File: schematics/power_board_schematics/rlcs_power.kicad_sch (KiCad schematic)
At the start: 40 parts, among them J1 Conn_01x05_Male, J2 Conn_01x05_Male, J3 Screw_Terminal_01x02, J4 Screw_Terminal_01x03, J5 Actuator Battery Conn, J6 Screw_Terminal_01x02, J7 Screw_Terminal_01x02, J8 Keylock Switch Conn, J9 Screw_Terminal_01x03, Q1 Q_NPN_BEC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

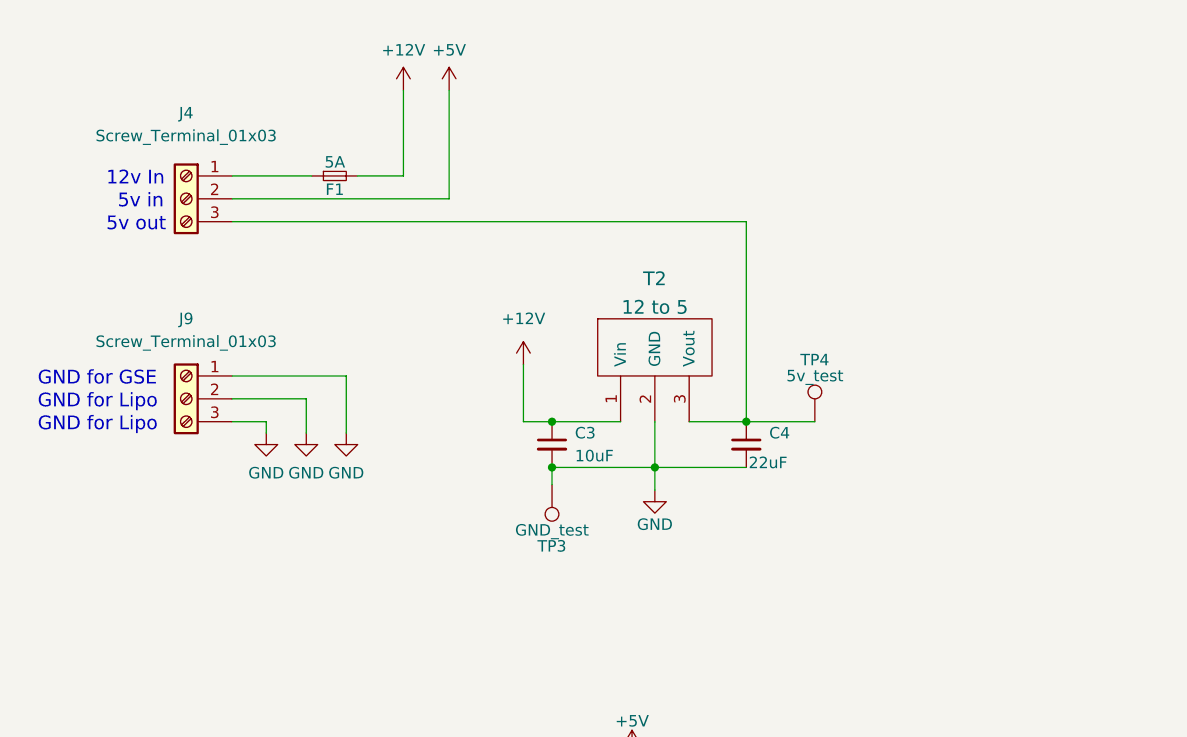
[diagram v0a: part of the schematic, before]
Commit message: Only use 12v power input for Towerside Power Board
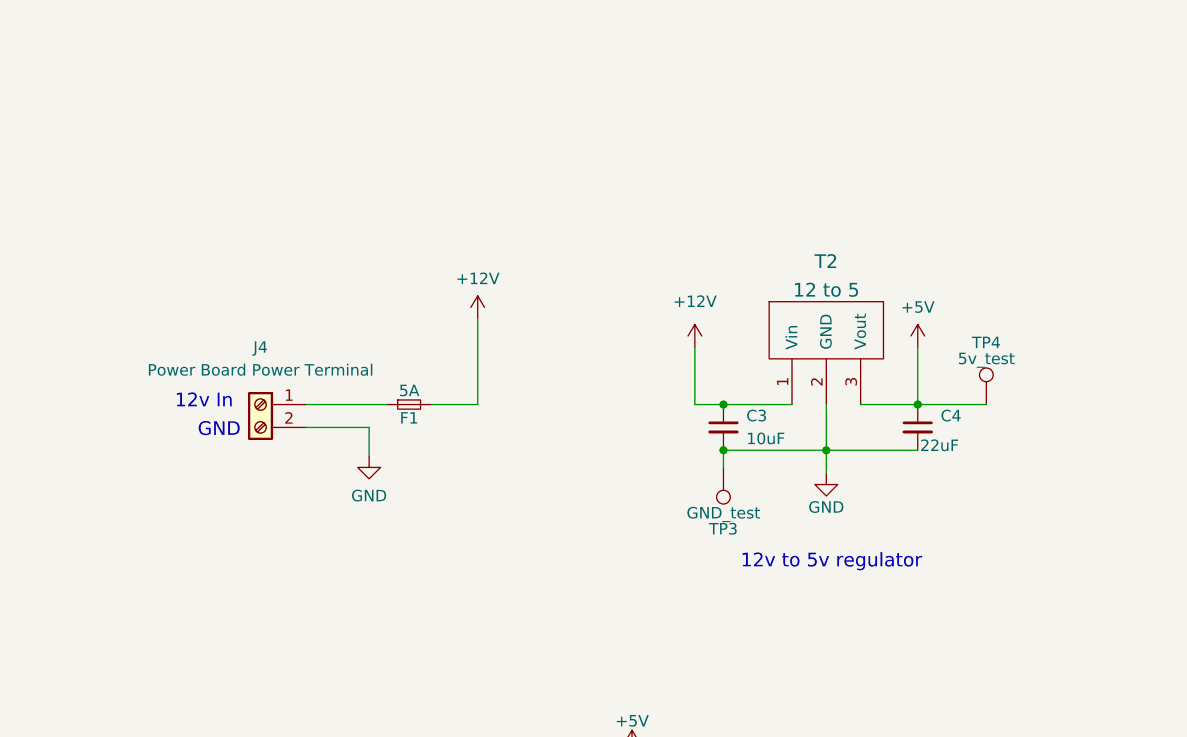
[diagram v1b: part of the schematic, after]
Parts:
- removed J4, J9: Screw_Terminal_01x03, TerminalBlock_Phoenix:TerminalBlock_Phoenix_MKDS-1,5-3-5.08_1x03_P5.08mm_Horizontal, symbol Connector:Screw_Terminal_01x03
- added J4: Power Board Power Terminal, symbol Connector:Screw_Terminal_01x02
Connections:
- net +5V: now also C4.1, T2.3 (Vout), TP4.1
- net GND: now also J4.2 (Pin_2)
- net at F1.1: now also J4.1 (Pin_1)
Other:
- note added: "12v to 5v regulator"
- note added: "GND"
- note removed: "5v in"
- note removed: "5v out"
- note removed: "GND for GSE"
- note removed: "GND for Lipo"
- moved on the sheet: C3, C4, F1, T2, TP3, TP4

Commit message: Organize Towerside Power Board schematic
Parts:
- J3: value Screw_Terminal_01x02 -> UART Conn
- J4: value Power Board Power Terminal -> Power Board Power Input
- J6: value Screw_Terminal_01x02 -> 12v Output
- J7: value Screw_Terminal_01x02 -> 5v Output
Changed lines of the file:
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@@
   (title_block
     (title "RLCS power board")
-    (date "2022-10-10")
+    (date "2022-10-11")
     (rev "A")
     (company "Waterloo Rocketry")
@@
     (stroke (width 0) (type default) (color 0 0 0 0))
   )
-  (wire (pts (xy 41.91 162.56) (xy 49.53 162.56))
-    (stroke (width 0) (type default) (color 0 0 0 0))
-  )
   (wire (pts (xy 57.15 162.56) (xy 59.69 162.56))
     (stroke (width 0) (type default) (color 0 0 0 0))
@@
     (stroke (width 0) (type default) (color 0 0 0 0))
   )
-  (wire (pts (xy 40.64 102.87) (xy 68.58 102.87))
-    (stroke (width 0) (type default) (color 0 0 0 0))
-  )
   (wire (pts (xy 96.52 59.055) (xy 104.14 59.055))
     (stroke (width 0) (type default) (color 0 0 0 0))
@@
     (stroke (width 0) (type default) (color 0 0 0 0))
   )
+  (wire (pts (xy 38.1 102.87) (xy 68.58 102.87))
+    (stroke (width 0) (type default) (color 0 0 0 0))
+  )
   (wire (pts (xy 139.7 151.13) (xy 139.7 158.75))
     (stroke (width 0) (type default) (color 0 0 0 0))
@@
   )
   (wire (pts (xy 254 26.67) (xy 254 27.305))
+    (stroke (width 0) (type default) (color 0 0 0 0))
+  )
+  (wire (pts (xy 38.1 162.56) (xy 49.53 162.56))
     (stroke (width 0) (type default) (color 0 0 0 0))
   )
@@
     )
   )
-  (global_label "Sevenseg_D1" (shape input) (at 41.91 162.56 180) (fields_autoplaced)
+  (global_label "Sevenseg_D1" (shape input) (at 38.1 162.56 180) (fields_autoplaced)
     (effects (font (size 1.524 1.524)) (justify right))
-    (property "Intersheet References" "${INTERSHEET_REFS}" (id 0) (at 24.4617 162.4648 0)
+    (property "Intersheet References" "${INTERSHEET_REFS}" (id 0) (at 20.6517 162.4648 0)
       (effects (font (size 1.524 1.524)) (justify right) hide)
     )
@@
     )
   )
-  (global_label "Sevenseg_D2" (shape input) (at 40.64 102.87 180) (fields_autoplaced)
+  (global_label "Sevenseg_D2" (shape input) (at 38.1 102.87 180) (fields_autoplaced)
     (effects (font (size 1.524 1.524)) (justify right))
-    (property "Intersheet References" "${INTERSHEET_REFS}" (id 0) (at 23.1917 102.7748 0)
+    (property "Intersheet References" "${INTERSHEET_REFS}" (id 0) (at 20.6517 102.7748 0)
       (effects (font (size 1.524 1.524)) (justify right) hide)
     )
@@
   (symbol (lib_id "Connector:Screw_Terminal_01x02") (at 254 85.09 0) (unit 1)
     (in_bom yes) (on_board yes) (fields_autoplaced)
-    (property "Reference" "J6" (id 0) (at 257.175 85.0899 0)
-      (effects (font (size 1.27 1.27)) (justify left))
-    )
-    (property "Value" "Screw_Terminal_01x02" (id 1) (at 257.175 87.6299 0)
+    (property "Reference" "J6" (id 0) (at 256.54 85.0899 0)
+      (effects (font (size 1.27 1.27)) (justify left))
+    )
+    (property "Value" "12v Output" (id 1) (at 256.54 87.6299 0)
       (effects (font (size 1.27 1.27)) (justify left))
     )
@@
   (symbol (lib_id "Connector:Screw_Terminal_01x02") (at 254 104.14 0) (unit 1)
     (in_bom yes) (on_board yes) (fields_autoplaced)
-    (property "Reference" "J7" (id 0) (at 257.175 104.1399 0)
-      (effects (font (size 1.27 1.27)) (justify left))
-    )
-    (property "Value" "Screw_Terminal_01x02" (id 1) (at 257.175 106.6799 0)
+    (property "Reference" "J7" (id 0) (at 256.54 104.1399 0)
+      (effects (font (size 1.27 1.27)) (justify left))
+    )
+    (property "Value" "5v Output" (id 1) (at 256.54 106.6799 0)
       (effects (font (size 1.27 1.27)) (justify left))
     )
@@
     (in_bom yes) (on_board yes)
     (property "Reference" "J3" (id 0) (at 200.66 81.915 0))
-    (property "Value" "Screw_Terminal_01x02" (id 1) (at 200.66 83.82 0))
+    (property "Value" "UART Conn" (id 1) (at 200.66 83.82 0))
     (property "Footprint" "TerminalBlock_Phoenix:TerminalBlock_Phoenix_PT-1,5-2-5.0-H_1x02_P5.00mm_Horizontal" (id 2) (at 200.66 86.36 0)
       (effects (font (size 1.27 1.27)) hide)
@@
     (in_bom yes) (on_board yes)
     (property "Reference" "J4" (id 0) (at 45.085 52.705 0))
-    (property "Value" "Power Board Power Terminal" (id 1) (at 45.085 55.245 0))
+    (property "Value" "Power Board Power Input" (id 1) (at 45.085 55.245 0))
     (property "Footprint" "" (id 2) (at 45.085 59.055 0)
       (effects (font (size 1.27 1.27)) hide)
@@
     )
     (path "/dd654b78-9c0d-41b7-ad5c-a9ae8bc2ff19"
-      (reference "J3") (unit 1) (value "Screw_Terminal_01x02") (footprint "TerminalBlock_Phoenix:TerminalBlock_Phoenix_PT-1,5-2-5.0-H_1x02_P5.00mm_Horizontal")
+      (reference "J3") (unit 1) (value "UART Conn") (footprint "TerminalBlock_Phoenix:TerminalBlock_Phoenix_PT-1,5-2-5.0-H_1x02_P5.00mm_Horizontal")
     )
     (path "/e3210621-2453-4b97-995b-7e62372fc5ce"
-      (reference "J4") (unit 1) (value "Power Board Power Terminal") (footprint "")
+      (reference "J4") (unit 1) (value "Power Board Power Input") (footprint "")
     )
     (path "/b66cf642-a1dc-4e74-85e6-669f964b45aa"
@@
     )
     (path "/3ff96f21-873b-473c-a7ea-332f0c31db33"
-      (reference "J6") (unit 1) (value "Screw_Terminal_01x02") (footprint "TerminalBlock_Phoenix:TerminalBlock_Phoenix_PT-1,5-2-5.0-H_1x02_P5.00mm_Horizontal")
+      (reference "J6") (unit 1) (value "12v Output") (footprint "TerminalBlock_Phoenix:TerminalBlock_Phoenix_PT-1,5-2-5.0-H_1x02_P5.00mm_Horizontal")
     )
     (path "/da2d6250-170b-4eed-a591-d9e7815b184b"
-      (reference "J7") (unit 1) (value "Screw_Terminal_01x02") (footprint "TerminalBlock_Phoenix:TerminalBlock_Phoenix_PT-1,5-2-5.0-H_1x02_P5.00mm_Horizontal")
+      (reference "J7") (unit 1) (value "5v Output") (footprint "TerminalBlock_Phoenix:TerminalBlock_Phoenix_PT-1,5-2-5.0-H_1x02_P5.00mm_Horizontal")
     )
     (path "/0a81f968-d32d-4e4d-acbd-0519aedcf51c"

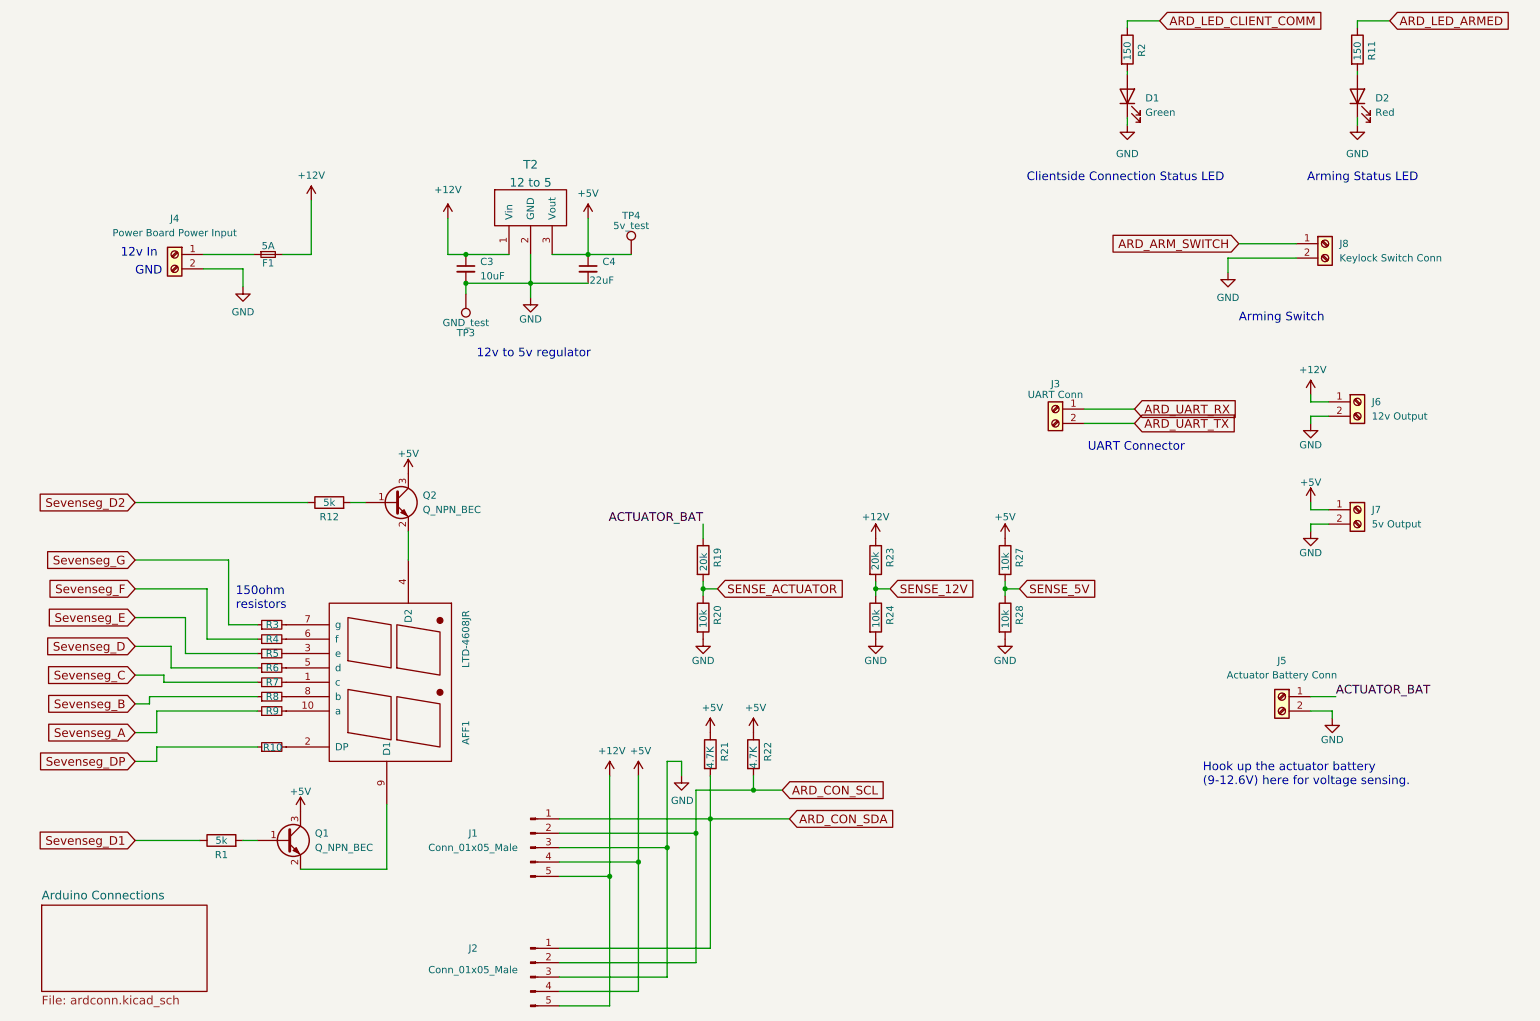
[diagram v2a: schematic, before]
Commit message: Update Power Board schematic based on Confluence documention
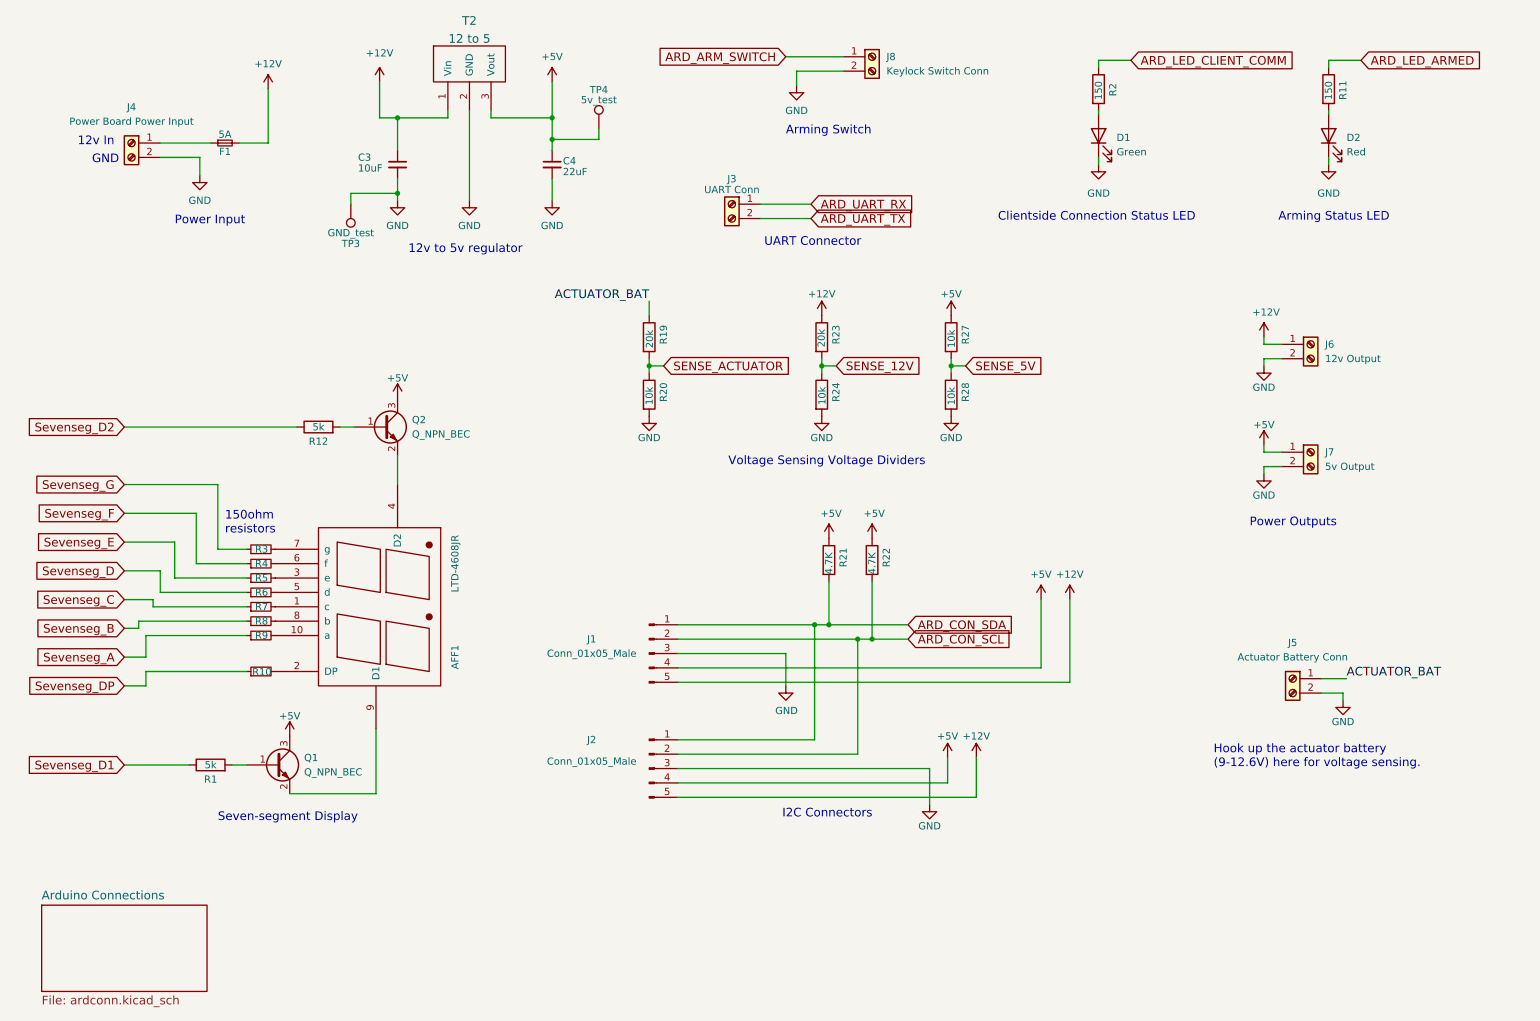
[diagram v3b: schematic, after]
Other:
- note added: "I2C Connectors"
- note added: "Power Input"
- note added: "Power Outputs"
- note added: "Seven-segment Display"
- note added: "Voltage Sensing Voltage Dividers"
- moved on the sheet: AFF1, C3, C4, D1, D2, F1, J1, J2, J3, J4, J5, J6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

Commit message: Fix test points layout on Towerside Power Board schematic
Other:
- note added: "Test points"
- moved on the sheet: C3, TP3, TP4
